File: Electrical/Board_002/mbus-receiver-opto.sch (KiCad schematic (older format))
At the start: 18 parts, among them J4 TEST_1P, J5 TEST_1P, U1 LTV-356T, U2 TSS721A

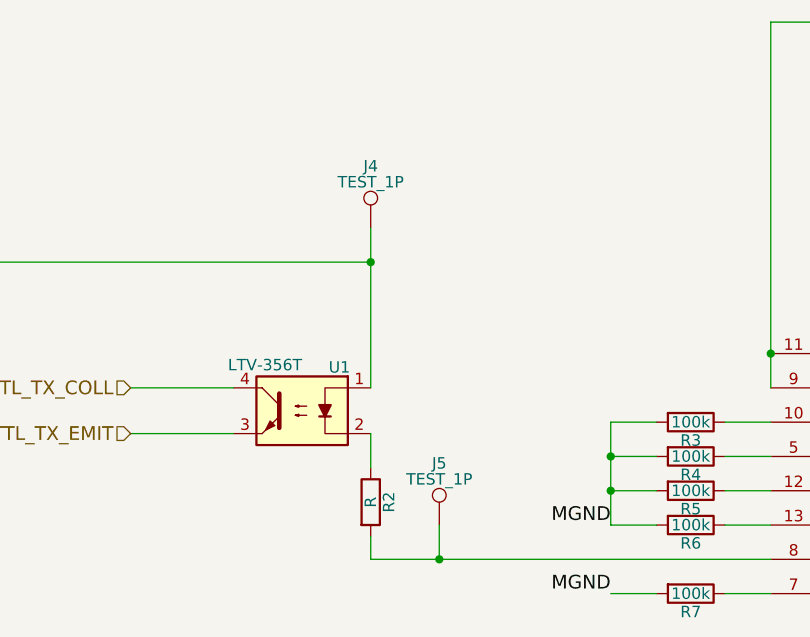
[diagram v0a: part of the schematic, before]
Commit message: Board_002: Add 2-pin connector to M-Bus
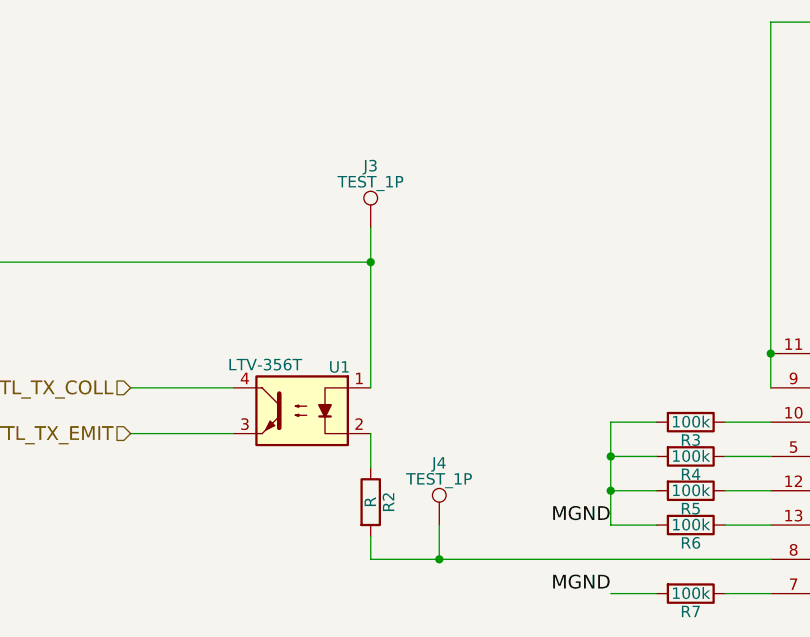
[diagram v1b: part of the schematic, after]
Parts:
- renumbered J4 to J3, J5 to J4
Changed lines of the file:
@@
 	4300 3450 4300 3300
 $Comp
-L TEST_1P J5
+L TEST_1P J4
 U 1 1 5A613111
 P 4600 3700
-F 0 "J5" H 4600 3970 50  0000 C CNN
+F 0 "J4" H 4600 3970 50  0000 C CNN
 F 1 "TEST_1P" H 4600 3900 50  0000 C CNN
 F 2 "" H 4800 3700 50  0001 C CNN
@@
 R_LOAD
 $Comp
-L TEST_1P J4
+L TEST_1P J3
 U 1 1 5A6141FE
 P 4300 2400
-F 0 "J4" H 4300 2670 50  0000 C CNN
+F 0 "J3" H 4300 2670 50  0000 C CNN
 F 1 "TEST_1P" H 4300 2600 50  0000 C CNN
 F 2 "" H 4500 2400 50  0001 C CNN
